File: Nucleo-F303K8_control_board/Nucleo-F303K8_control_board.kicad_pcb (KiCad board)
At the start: 2 copper layers, 55 x 70 mm, 33 parts, among them J1 Conn_01x02_Pin, J10 Conn_01x04_Pin, J11 Conn_01x04_Pin, J2 Conn_01x03_Pin, J3 Conn_01x03_Pin, J4 Conn_01x02_Pin, J5 Conn_01x02_Pin, J6 Conn_01x04_Pin, J7 Conn_01x03_Pin, J8 Conn_01x03_Pin, J9 Conn_01x03_Pin, U1 NUCLEO-F303K8, U2 MCP2562-E-P

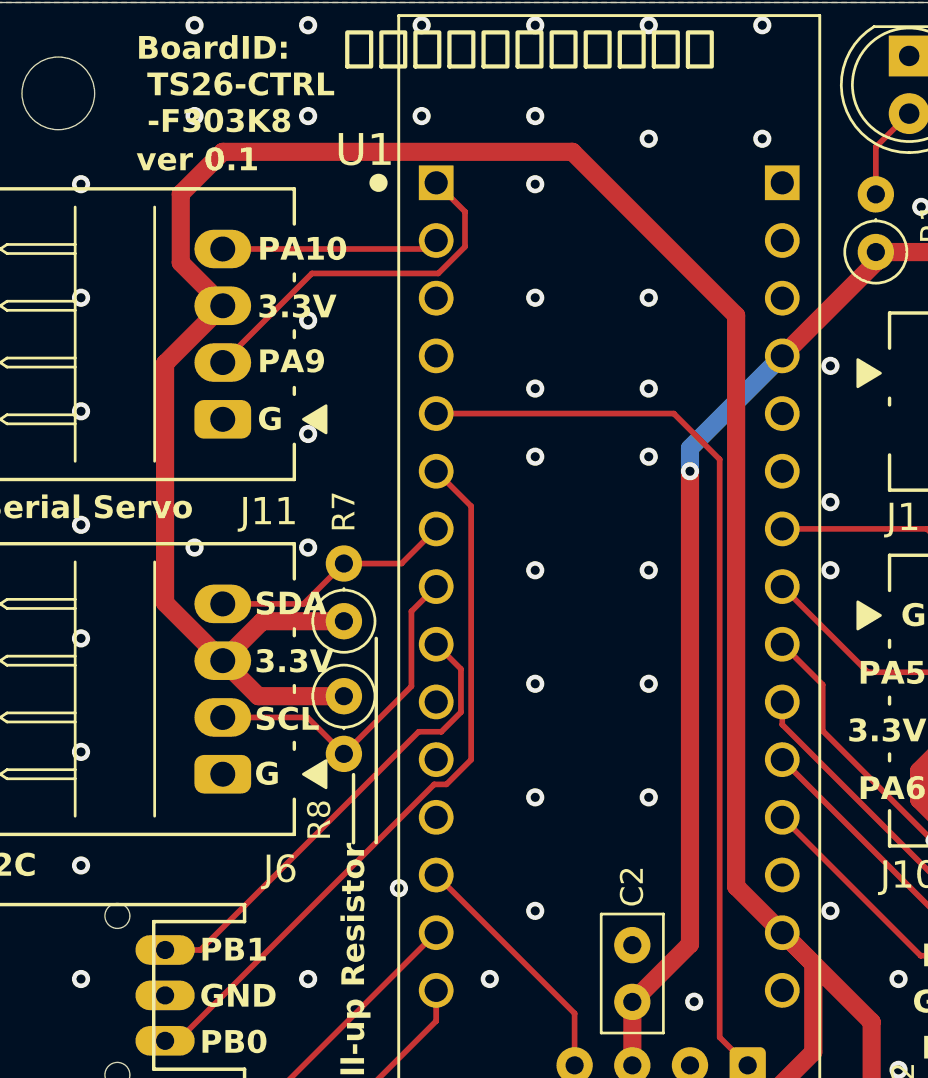
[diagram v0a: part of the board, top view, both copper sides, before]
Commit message: F303K8基板　シリアル通信端子の電源ピンを5Vに変更，ver 0.2
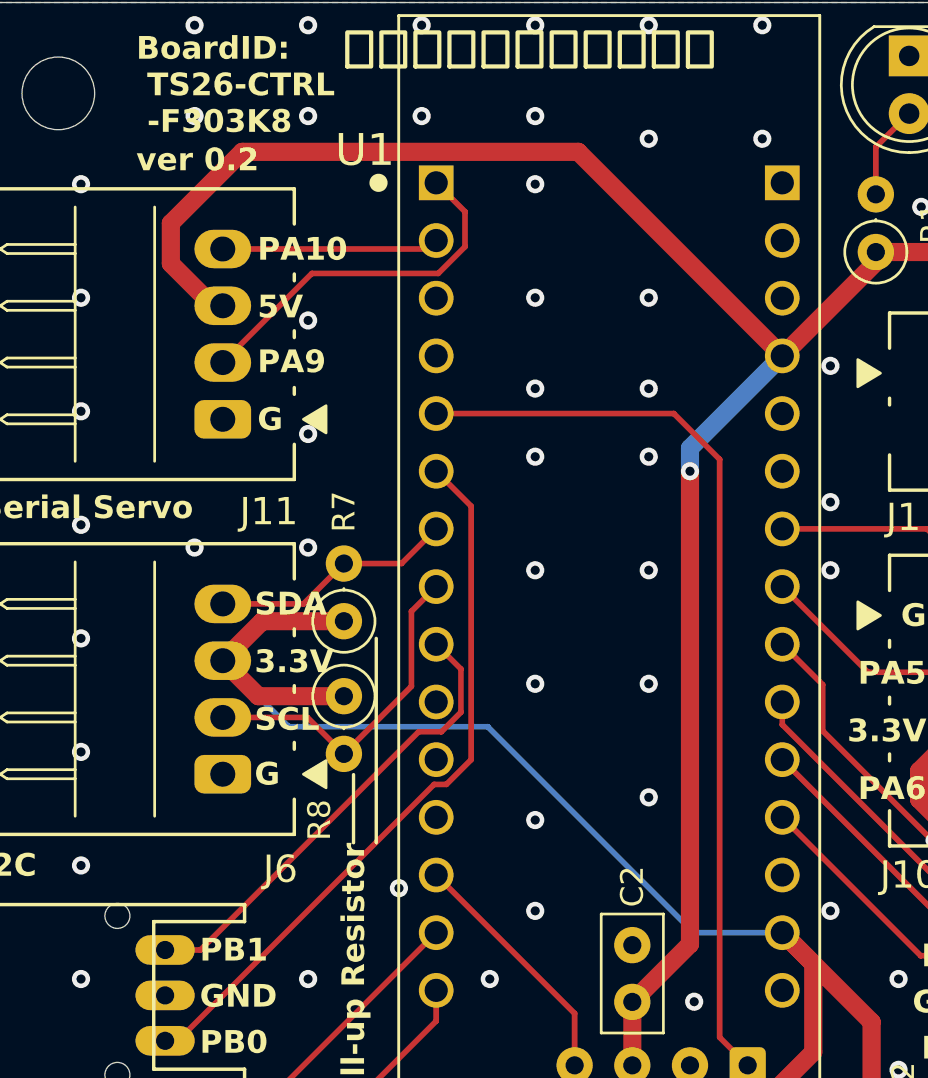
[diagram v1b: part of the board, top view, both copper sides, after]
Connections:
- J11 pad 3: +3.3V -> +5V
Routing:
- net +3.3V: track 184.5 -> 134.4 mm
- net +5V: track 56.9 -> 93.7 mm
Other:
- board text added: "5V"
- board text added: "ver 0.2"
- board text removed: "ver 0.1"
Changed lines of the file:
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@@
 			(layers "*.Cu" "*.Mask")
 			(remove_unused_layers no)
-			(net "+3.3V")
+			(net "+5V")
 			(pinfunction "Pin_3_3")
 			(pintype "passive")
@@
 		)
 	)
-	(gr_text "ver 0.1"
+	(gr_text "ver 0.2"
 		(at 27.432 26.924 0)
 		(layer "F.SilkS")
@@
 		)
 	)
-	(gr_text "3.3V"
+	(gr_text "5V"
 		(at 32.766 33.401 0)
 		(layer "F.SilkS" knockout)
@@
 	)
 	(via
-		(at 45 55)
+		(at 45 56)
 		(size 0.8)
 		(drill 0.4)
@@
 	)
 	(segment
-		(start 59.814 76.324)
-		(end 61.214 77.724)
+		(start 60 31.44)
+		(end 55.88 35.56)
 		(width 0.8)
 		(layer "F.Cu")
-		(net "+3.3V")
+		(net "+5V")
 	)
 	(segment
-		(start 53.848 33.782)
-		(end 53.848 58.928)
+		(start 60 30.988)
+		(end 60 31.44)
 		(width 0.8)
 		(layer "F.Cu")
-		(net "+3.3V")
+		(net "+5V")
 	)
 	(segment
-		(start 62.75339 55.94)
-		(end 61.904 55.09061)
+		(start 28.956 31.496)
+		(end 28.956 29.718)
 		(width 0.8)
 		(layer "F.Cu")
-		(net "+3.3V")
+		(net "+5V")
 	)
 	(segment
-		(start 53.848 58.928)
-		(end 55.88 60.96)
+		(start 31.242 33.354)
+		(end 31.242 33.30461)
 		(width 0.8)
 		(layer "F.Cu")
-		(net "+3.3V")
+		(net "+5V")
 	)
 	(segment
-		(start 70.612 70.933919)
-		(end 70.612 72.136)
+		(start 63.754 38.822)
+		(end 65.004 38.822)
 		(width 0.8)
 		(layer "F.Cu")
-		(net "+3.3V")
+		(net "+5V")
+	)
+	(segment
+		(start 51.816 40.64)
+		(end 51.816 61.468)
+		(width 0.8)
+		(layer "F.Cu")
+		(net "+5V")
+	)
+	(segment
+		(start 66.802 37.024)
+		(end 66.802 30.988)
+		(width 0.8)
+		(layer "F.Cu")
+		(net "+5V")
+	)
+	(segment
+		(start 51.816 61.468)
+		(end 49.276 64.008)
+		(width 0.8)
+		(layer "F.Cu")
+		(net "+5V")
+	)
+	(segment
+		(start 65.004 38.822)
+		(end 66.802 37.024)
+		(width 0.8)
+		(layer "F.Cu")
+		(net "+5V")
+	)
+	(segment
+		(start 49.276 64.008)
+		(end 49.276 66.802)
+		(width 0.8)
+		(layer "F.Cu")
+		(net "+5V")
+	)
+	(segment
+		(start 46.895 26.575)
+		(end 55.88 35.56)
+		(width 0.8)
+		(layer "F.Cu")
+		(net "+5V")
+	)
+	(segment
+		(start 66.802 30.988)
+		(end 60 30.988)
+		(width 0.8)
+		(layer "F.Cu")
+		(net "+5V")
+	)
+	(segment
+		(start 28.956 29.718)
+		(end 32.099 26.575)
+		(width 0.8)
+		(layer "F.Cu")
+		(net "+5V")
+	)
+	(segment
+		(start 32.099 26.575)
+		(end 46.895 26.575)
+		(width 0.8)
+		(layer "F.Cu")
+		(net "+5V")
+	)
+	(segment
+		(start 30.814 33.354)
+		(end 28.956 31.496)
+		(width 0.8)
+		(layer "F.Cu")
+		(net "+5V")
+	)
+	(segment
+		(start 31.242 33.354)
+		(end 30.814 33.354)
+		(width 0.8)
+		(layer "F.Cu")
+		(net "+5V")
+	)
+	(via
+		(at 51.816 40.64)
+		(size 0.8)
+		(drill 0.4)
+		(layers "F.Cu" "B.Cu")
+		(net "+5V")
+	)
+	(segment
+		(start 55.88 35.56)
+		(end 51.816 39.624)
+		(width 0.8)
+		(layer "B.Cu")
+		(net "+5V")
+	)
+	(segment
+		(start 51.816 39.624)
+		(end 51.816 40.64)
+		(width 0.8)
+		(layer "B.Cu")
+		(net "+5V")
+	)
+	(segment
+		(start 40.266 30.854)
+		(end 40.64 30.48)
+		(width 0.25)
+		(layer "F.Cu")
+		(net "/PA10")
 	)
 	(segment
-		(start 28.702 35.894)
-		(end 28.702 46.442)
+		(start 31.242 30.854)
+		(end 40.266 30.854)
+		(width 0.25)
+		(layer "F.Cu")
+		(net "/PA10")
+	)
+	(segment
+		(start 64.516 72.136)
+		(end 61.214 72.136)
+		(width 0.25)
+		(layer "F.Cu")
+		(net "Net-(J2-Pin_1)")
+	)
+	(segment
+		(start 68.072 72.136)
+		(end 64.516 72.136)
+		(width 0.25)
+		(layer "F.Cu")
+		(net "Net-(J2-Pin_1)")
+	)
+	(segment
+		(start 58.166 72.136)
+		(end 57.658 72.644)
+		(width 0.25)
+		(layer "B.Cu")
+		(net "Net-(J2-Pin_1)")
+	)
+	(segment
+		(start 61.214 72.136)
+		(end 58.166 72.136)
+		(width 0.25)
+		(layer "B.Cu")
+		(net "Net-(J2-Pin_1)")
+	)
+	(segment
+		(start 59.814 76.324)
+		(end 61.214 77.724)
 		(width 0.8)
 		(layer "F.Cu")
@@
 	)
 	(segment
-		(start 59.814 64.894)
-		(end 59.814 68.196)
+		(start 62.75339 55.94)
+		(end 61.904 55.09061)
 		(width 0.8)
 		(layer "F.Cu")
@@
 	)
 	(segment
-		(start 61.214 77.724)
-		(end 68.432 77.724)
+		(start 70.612 70.933919)
+		(end 70.612 72.136)
 		(width 0.8)
 		(layer "F.Cu")
@@
 	)
 	(segment
-		(start 31.242 33.354)
-		(end 28.702 35.894)
+		(start 59.814 64.894)
+		(end 59.814 68.196)
 		(width 0.8)
 		(layer "F.Cu")
@@
 	)
 	(segment
-		(start 46.641 26.575)
-		(end 53.848 33.782)
+		(start 61.214 77.724)
+		(end 68.432 77.724)
 		(width 0.8)
 		(layer "F.Cu")
@@
 	)
 	(segment
-		(start 31.242 33.354)
-		(end 31.242 33.30461)
-		(width 0.8)
-		(layer "F.Cu")
-		(net "+3.3V")
-	)
-	(segment
-		(start 29.392 28.425)
-		(end 31.242 26.575)
-		(width 0.8)
-		(layer "F.Cu")
-		(net "+3.3V")
-	)
-	(segment
 		(start 57.245 66.22201)
 		(end 50.44501 73.022)
@@
 	)
 	(segment
-		(start 31.242 26.575)
-		(end 46.641 26.575)
-		(width 0.8)
-		(layer "F.Cu")
-		(net "+3.3V")
-	)
-	(segment
-		(start 28.702 46.442)
-		(end 31.242 48.982)
-		(width 0.8)
-		(layer "F.Cu")
-		(net "+3.3V")
-	)
-	(segment
 		(start 65.809056 55.94)
 		(end 62.75339 55.94)
@@
 	)
 	(segment
-		(start 31.242 33.30461)
-		(end 29.392 31.45461)
-		(width 0.8)
-		(layer "F.Cu")
-		(net "+3.3V")
-	)
-	(segment
 		(start 59.814 68.196)
 		(end 59.814 76.324)
@@
 	)
 	(segment
-		(start 29.392 31.45461)
-		(end 29.392 28.425)
-		(width 0.8)
-		(layer "F.Cu")
-		(net "+3.3V")
-	)
-	(segment
 		(start 69.848 59.978944)
 		(end 65.809056 55.94)
@@
 	)
 	(segment
-		(start 40.266 30.854)
-		(end 40.64 30.48)
-		(width 0.25)
-		(layer "F.Cu")
-		(net "/PA10")
-	)
-	(segment
-		(start 31.242 30.854)
-		(end 40.266 30.854)
-		(width 0.25)
-		(layer "F.Cu")
-		(net "/PA10")
-	)
-	(segment
-		(start 64.516 72.136)
-		(end 61.214 72.136)
-		(width 0.25)
-		(layer "F.Cu")
-		(net "Net-(J2-Pin_1)")
-	)
-	(segment
-		(start 68.072 72.136)
-		(end 64.516 72.136)
-		(width 0.25)
-		(layer "F.Cu")
-		(net "Net-(J2-Pin_1)")
-	)
-	(segment
-		(start 58.166 72.136)
-		(end 57.658 72.644)
+		(start 55.88 60.96)
+		(end 51.985305 60.96)
 		(width 0.25)
 		(layer "B.Cu")
-		(net "Net-(J2-Pin_1)")
+		(net "+3.3V")
 	)
 	(segment
-		(start 61.214 72.136)
-		(end 58.166 72.136)
+		(start 42.915305 51.89)
+		(end 34.15 51.89)
 		(width 0.25)
 		(layer "B.Cu")
-		(net "Net-(J2-Pin_1)")
-	)
-	(segment
-		(start 60 31.44)
-		(end 55.88 35.56)
-		(width 0.8)
-		(layer "F.Cu")
-		(net "+5V")
-	)
-	(segment
-		(start 60 30.988)
-		(end 60 31.44)
-		(width 0.8)
-		(layer "F.Cu")
-		(net "+5V")
-	)
-	(segment
-		(start 63.754 38.822)
-		(end 65.004 38.822)
-		(width 0.8)
-		(layer "F.Cu")
-		(net "+5V")
-	)
-	(segment
-		(start 51.816 40.64)
-		(end 51.816 61.468)
-		(width 0.8)
-		(layer "F.Cu")
-		(net "+5V")
-	)
-	(segment
-		(start 66.802 37.024)
-		(end 66.802 30.988)
-		(width 0.8)
-		(layer "F.Cu")
-		(net "+5V")
-	)
-	(segment
-		(start 51.816 61.468)
-		(end 49.276 64.008)
-		(width 0.8)
-		(layer "F.Cu")
-		(net "+5V")
-	)
-	(segment
-		(start 65.004 38.822)
-		(end 66.802 37.024)
-		(width 0.8)
-		(layer "F.Cu")
-		(net "+5V")
-	)
-	(segment
-		(start 49.276 64.008)
-		(end 49.276 66.802)
-		(width 0.8)
-		(layer "F.Cu")
-		(net "+5V")
-	)
-	(segment
-		(start 66.802 30.988)
-		(end 60 30.988)
-		(width 0.8)
-		(layer "F.Cu")
-		(net "+5V")
-	)
-	(via
-		(at 51.816 40.64)
-		(size 0.8)
-		(drill 0.4)
-		(layers "F.Cu" "B.Cu")
-		(net "+5V")
+		(net "+3.3V")
 	)
 	(segment
-		(start 55.88 35.56)
-		(end 51.816 39.624)
-		(width 0.8)
+		(start 51.985305 60.96)
+		(end 42.915305 51.89)
+		(width 0.25)
 		(layer "B.Cu")
-		(net "+5V")
+		(net "+3.3V")
 	)
 	(segment
-		(start 51.816 39.624)
-		(end 51.816 40.64)
-		(width 0.8)
+		(start 34.15 51.89)
+		(end 31.242 48.982)
+		(width 0.25)
 		(layer "B.Cu")
-		(net "+5V")
+		(net "+3.3V")
 	)
 	(segment
